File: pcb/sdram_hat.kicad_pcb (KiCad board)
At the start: 2 copper layers, 76.2 x 76.2 mm, 34 parts, among them J1 CONN_02X20, J2 CONN_02X20, J3 CONN_02X20, J4 CONN_02X20, J5 AUDIO_OUT_JACK

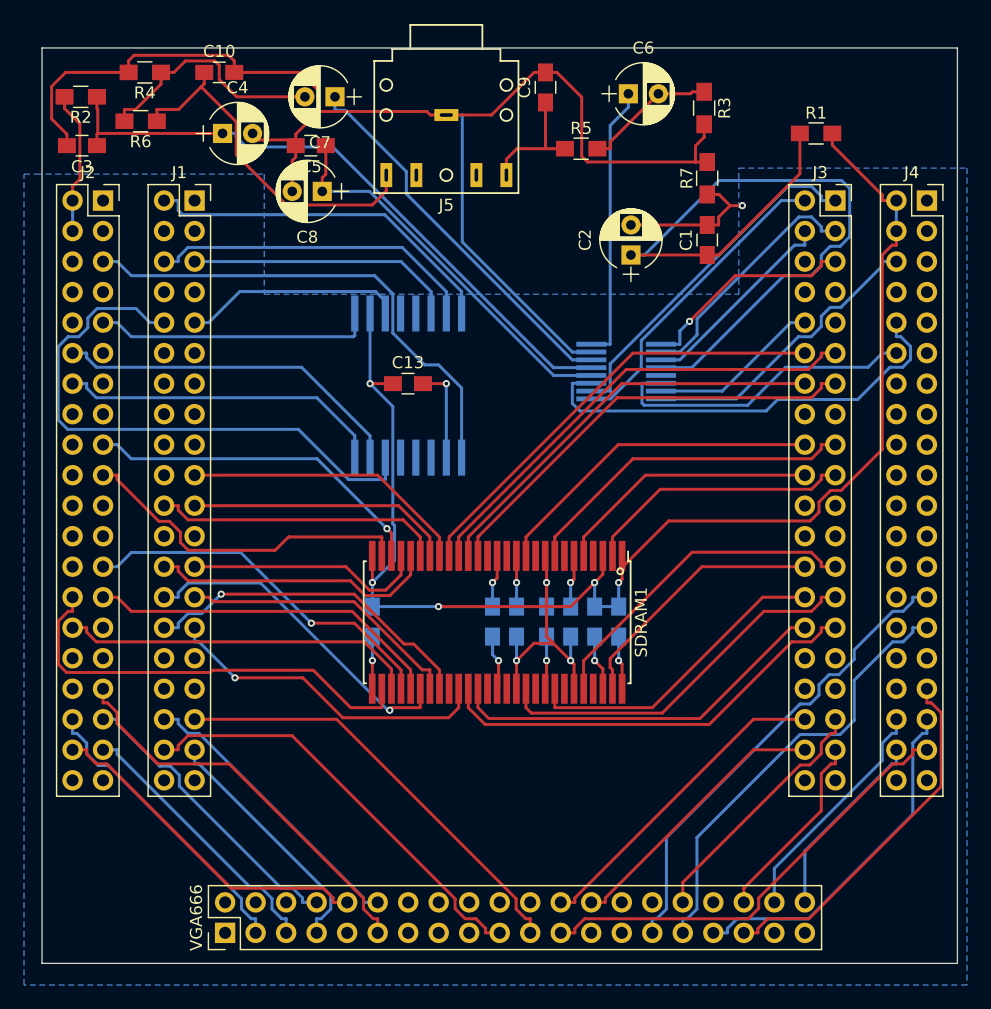
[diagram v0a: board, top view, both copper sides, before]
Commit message: Fix footprint cuts for audio jack
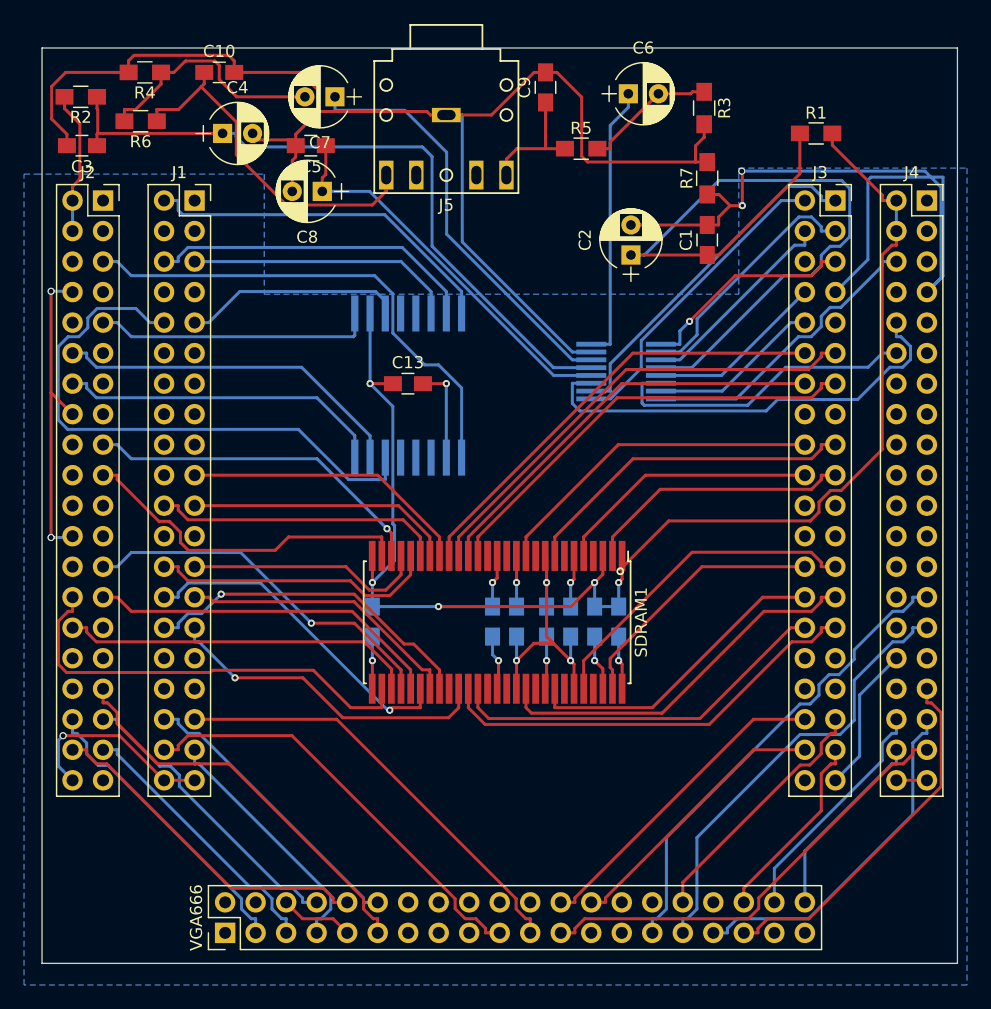
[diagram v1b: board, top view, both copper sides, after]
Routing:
- net GND: track 51.7 -> 187.2 mm, vias 9 -> 13
- net Net-(AUDIO_ENC1-Pad13): track 53.4 -> 57.8 mm
- net Net-(AUDIO_ENC1-Pad14): track 32.2 -> 35.1 mm

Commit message: Length match QPI flash and SDRAM traces
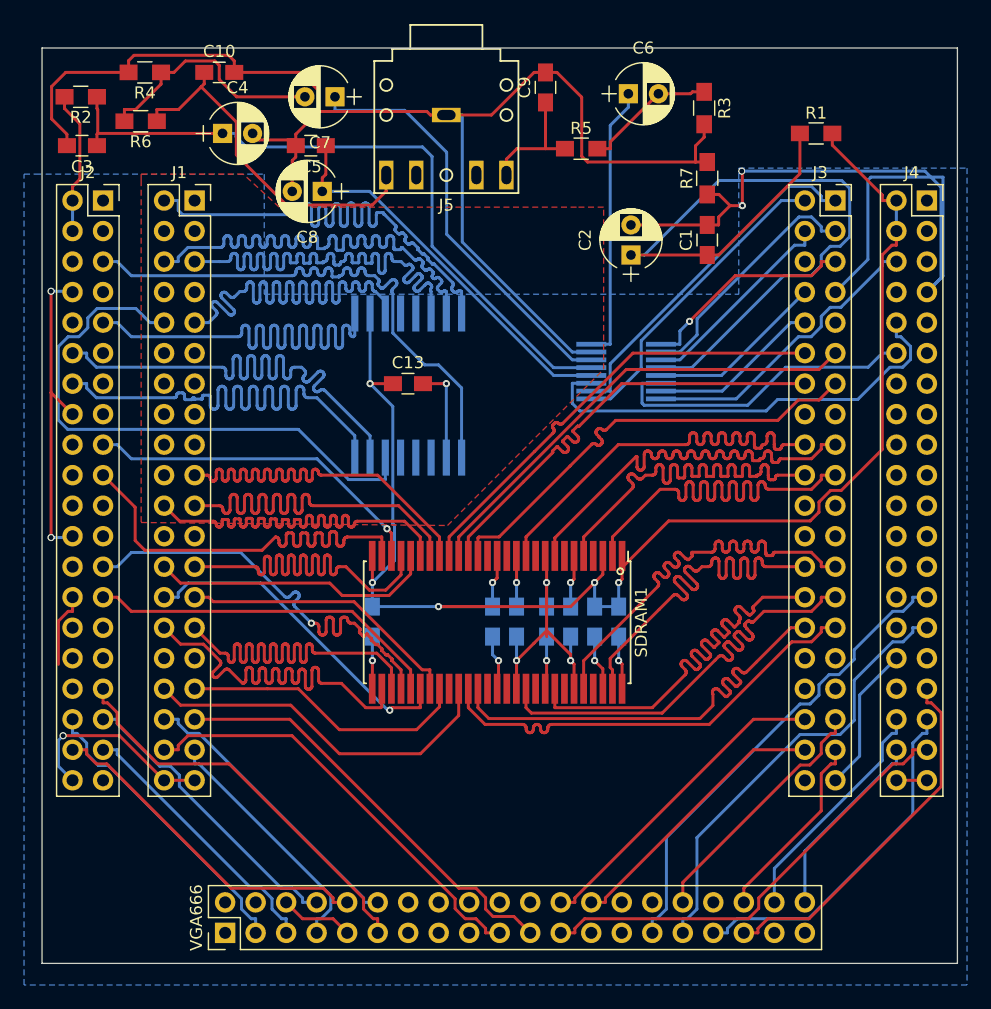
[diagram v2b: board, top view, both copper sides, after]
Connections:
- SDRAM1 pad 29: G16 -> A5
- SDRAM1 pad 30: F16 -> C4
- SDRAM1 pad 35: A5 -> C3
- SDRAM1 pad 37: C4 -> B5
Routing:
- net B5: track 0.00 -> 30.3 mm
- net G16: track 36.4 -> 6.29 mm
- net F16: track 29.8 -> 0.00 mm
- net B11: track 18.3 -> 48.0 mm
- net B14: track 22.5 -> 48.1 mm
- net M15: track 23.3 -> 48.0 mm
- net C3: track 0.00 -> 24.1 mm
- net K15: track 27.3 -> 48.1 mm
- net B13: track 27.5 -> 48.1 mm
- net M16: track 29.7 -> 48.0 mm
- net A16: track 30.2 -> 48.2 mm
- net C6: track 20.1 -> 38.0 mm
- net P8: track 22.1 -> 38.2 mm
- net SDRAM_D7: track 22.0 -> 38.0 mm
- net C7: track 22.2 -> 38.0 mm
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- added copper zone on F.Cu, net GND

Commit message: Very misalign. Wow. Much fix.
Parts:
- moved J3 2.04 mm to (79.2, 27.9)
- moved J1 1.14 mm to (29.1, 27.9)
- moved J4 0.87 mm to (88.0, 27.9)
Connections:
- QPI_FLASH1 pad 1: M15 -> B11
- QPI_FLASH1 pad 14: B12 -> A11
- QPI_FLASH1 pad 15: M16 -> C9
- QPI_FLASH1 pad 3: B11 -> B12
- QPI_FLASH1 pad 9: P15 -> B9
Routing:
- net GND: track 187.2 -> 271.0 mm, vias 13 -> 14
- net P15: track 48.1 -> 0.00 mm
- net M15: track 48.0 -> 0.00 mm
- net M16: track 48.0 -> 1.20 mm
- net Net-(AUDIO_ENC1-Pad4): track 66.0 -> 32.0 mm
- net A11: track 0.00 -> 29.3 mm
- net B9: track 0.00 -> 28.2 mm
- net C9: track 0.00 -> 28.2 mm
- net +3V3: track 149.7 -> 174.1 mm
- net B12: track 48.3 -> 28.2 mm
- net A16: track 48.2 -> 28.2 mm
- net B14: track 48.1 -> 28.2 mm
- net B13: track 48.1 -> 28.2 mm
- net K15: track 48.1 -> 28.2 mm
- net B11: track 48.0 -> 28.2 mm
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
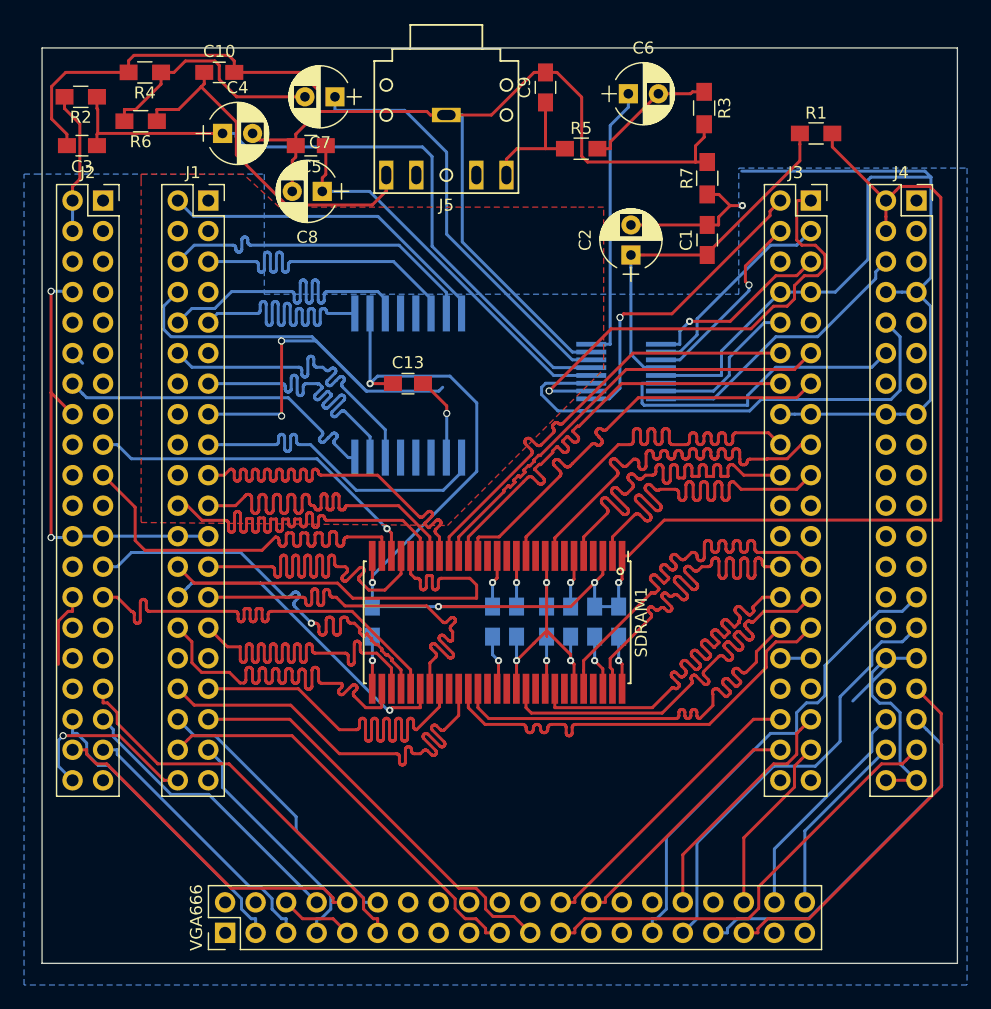
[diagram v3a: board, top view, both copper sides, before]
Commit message: Updated NES-Hat PCB to rev 2
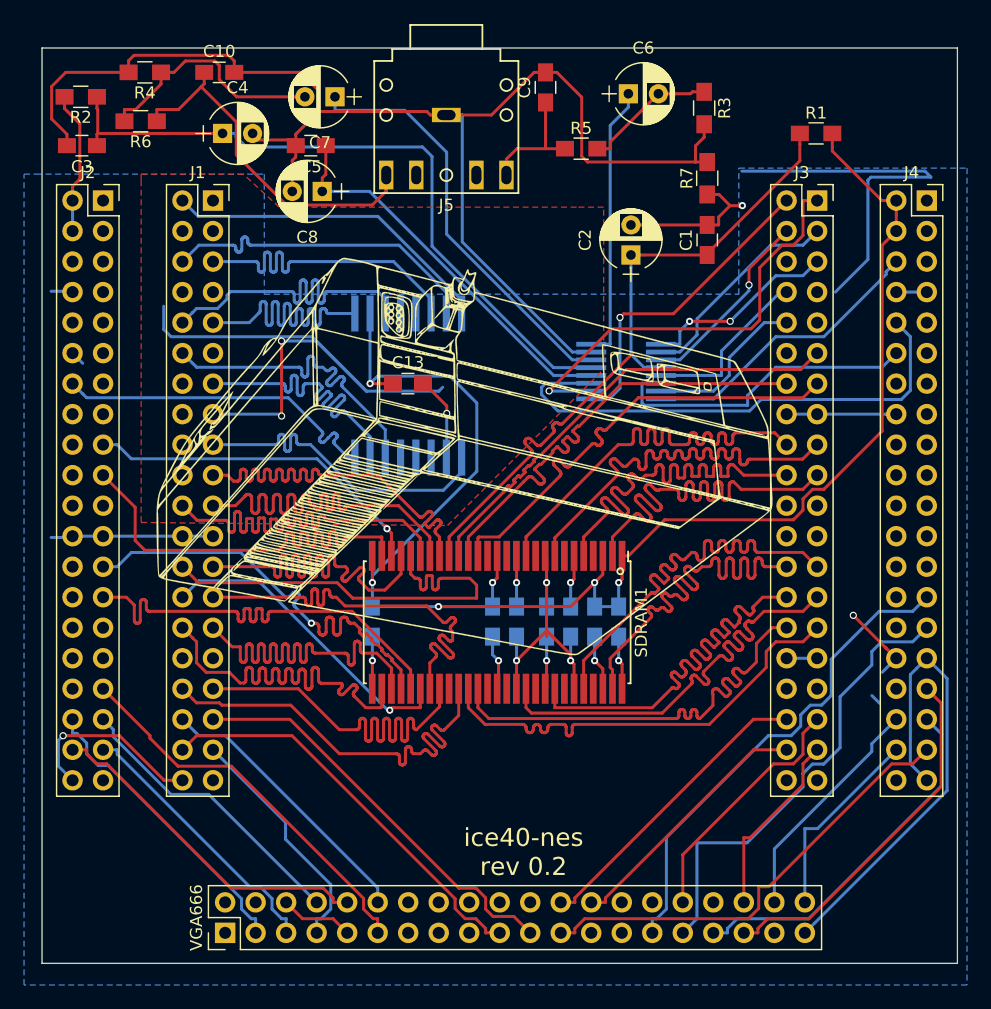
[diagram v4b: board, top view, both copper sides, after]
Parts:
- added G***: LOGO, pcb:nes_console_scaled, F.Cu at (50.8, 49.6)
- moved J4 0.86 mm to (88.9, 27.9)
- moved J3 0.52 mm to (79.8, 27.9)
- moved J1 0.39 mm to (29.5, 27.9)
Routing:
- net GND: track 271.0 -> 210.4 mm, vias 14 -> 13
- net (no net): track 0.00 -> 32.6 mm
- net +3V3: track 174.1 -> 158.7 mm
- net N10: track 38.0 -> 25.7 mm
- net G16: track 6.29 -> 0.00 mm
- net DAC_PLL0: track 39.8 -> 36.6 mm
- net F1: track 36.9 -> 38.3 mm
- net A7: track 37.9 -> 36.7 mm
- net D15: track 33.7 -> 32.6 mm
- net B1: track 15.5 -> 16.5 mm
- net SDRAM_DM: track 38.0 -> 38.9 mm
- net F14: track 38.0 -> 37.1 mm
- net DAC_SYSCLK: track 25.9 -> 26.7 mm
- net DAC_SFOR0: track 42.4 -> 43.2 mm
- net A2: track 35.2 -> 34.4 mm
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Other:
- board text added: "ice40-nes rev 0.2"
